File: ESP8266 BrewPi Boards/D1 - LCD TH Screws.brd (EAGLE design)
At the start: 46.9 x 57.5 mm, 10 parts, among them J1 RJ45-8X

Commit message: Updating TH Screw board
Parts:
- added C1, C3: 0.1uF, rcl:C050-035X075
- added C2, C4: 1uF, rcl:C050-035X075
- added ONEWIRE_VSEL: (no value), jumper:SJ_2W
- moved R1 1.91 mm to (31.8, 12.1), turned to 180 degrees
- moved U$3 1.27 mm to (9.53, 26.7)
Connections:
- new net N$3: J1.3, ONEWIRE_VSEL.2
- net 3V3: now also C3.1, C4.1, ONEWIRE_VSEL.3; no longer J1.3
- net 5V: now also C1.2, C2.2, ONEWIRE_VSEL.1
- net GND: now also C1.1, C2.1, C3.2, C4.2
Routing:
- net GND: track 34.1 -> 180.9 mm
- net N$3: track 0.00 -> 18.9 mm
- net 3V3: track 59.8 -> 75.5 mm
- net ONEWIRE: track 37.4 -> 22.6 mm
- net 5V: track 124.6 -> 138.7 mm
- net N$2: track 47.0 -> 45.2 mm
- net N$1: track 49.5 -> 47.7 mm
- net N$5: track 26.9 -> 26.2 mm
- net N$4: track 29.3 -> 28.8 mm
- net DOOR: track 15.0 -> 14.5 mm
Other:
- outline, holes or cut-outs redrawn
- board text added: "0.1uF"
- board text added: "1uF"
- board text added: "3V3"
- board text added: "4.7k"
- board text added: "5V"
- board text added: "BrewPi D1 Mini TH Screws - v1.1 @thorrak says hi"
- board text added: "COOL"
- board text added: "D0 - Heat D1 - I2C SCL D2 - I2C SDA D5 - Cool D6 - OneWire Data D7 - Door"
- board text added: "HEAT"
- board text added: "OW"
- board text removed: "BrewPi D1 Mini TH Screws - v0.2 @thorrak says hi"
- board text removed: "D0 (HEAT)"
- board text removed: "D0 - Heat D1 - I2C SCL D2 - I2C SDA D3 - Buzzer D5 - Cool D6 - OneWire Data D7 - Door"
- board text removed: "D5 (COOL)"

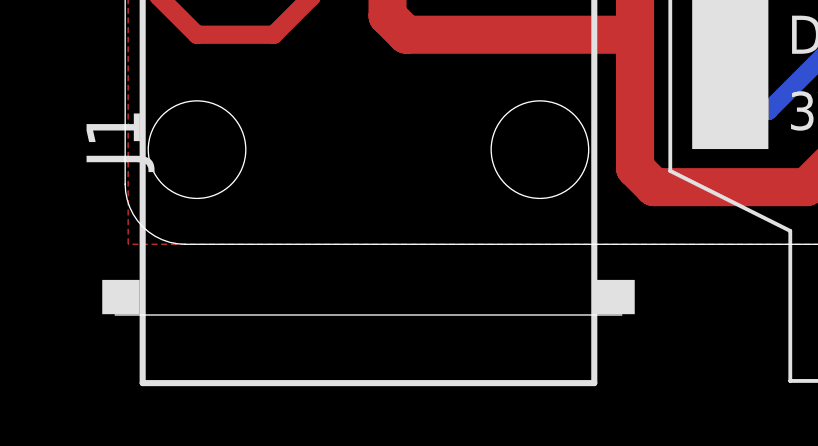
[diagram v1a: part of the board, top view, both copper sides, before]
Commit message: Updating board designs and adding DirtyPCB Links
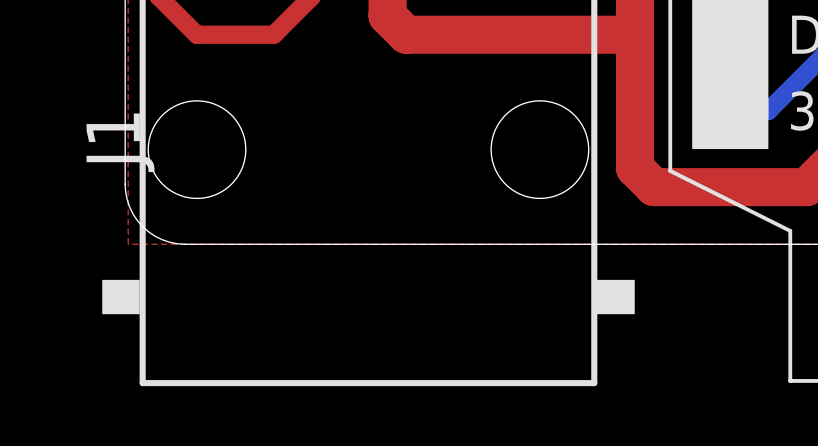
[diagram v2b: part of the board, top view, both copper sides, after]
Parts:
- J1: device con-tycoelectronics:RJ45-NO-SHIELD -> Donnie:RJ45-NS-XDIM
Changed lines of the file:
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@@
 <layer number="59" name="tCarbon" color="7" fill="1" visible="no" active="no"/>
 <layer number="60" name="bCarbon" color="7" fill="1" visible="no" active="no"/>
+<layer number="88" name="SimResults" color="9" fill="1" visible="no" active="no"/>
+<layer number="89" name="SimProbes" color="9" fill="1" visible="no" active="no"/>
 <layer number="90" name="Modules" color="5" fill="1" visible="no" active="no"/>
 <layer number="91" name="Nets" color="2" fill="1" visible="no" active="no"/>
@@
 <layer number="230" name="230bmp" color="7" fill="1" visible="no" active="yes"/>
 <layer number="231" name="231bmp" color="7" fill="1" visible="no" active="yes"/>
+<layer number="232" name="Eagle3D_PG2" color="7" fill="1" visible="no" active="no"/>
+<layer number="233" name="Eagle3D_PG3" color="7" fill="1" visible="no" active="no"/>
 <layer number="248" name="Housing" color="7" fill="1" visible="no" active="yes"/>
 <layer number="249" name="Edge" color="7" fill="1" visible="no" active="yes"/>
@@
 <attribute name="VALUE" x="37.465" y="41.235" size="1.27" layer="27" ratio="10" rot="R270"/>
 </element>
-<element name="J1" library="con-tycoelectronics" library_urn="urn:adsk.eagle:library:193" package="RJ45-NO-SHIELD" package3d_urn="urn:adsk.eagle:package:10660/1" value="RJ45-8X" x="8.26" y="3.155" smashed="yes">
+<element name="J1" library="Donnie" package="RJ45-NS-XDIM" package3d_urn="urn:adsk.eagle:package:10660/1" value="RJ45-8X" x="8.26" y="3.155" smashed="yes">
 <attribute name="MF" value="" x="8.26" y="3.155" size="1.778" layer="27" display="off"/>
 <attribute name="MPN" value="RJ45-8X" x="8.26" y="3.155" size="1.778" layer="27" display="off"/>
